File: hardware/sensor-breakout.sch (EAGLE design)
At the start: 63 parts, among them IC1 ATMEGA168-MU, U1 MCP73831, U2 NRF24L01SMD, U4 MCP5301, Y1 16M, Y2 12MHz

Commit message: hw: update values
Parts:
- R1: value TBD -> 3k9
- R2: value 2k2 -> 1k5
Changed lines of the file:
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@@
 <part name="GND6" library="supply1" deviceset="GND" device=""/>
 <part name="GND2" library="supply1" deviceset="GND" device=""/>
-<part name="R2" library="rcl" deviceset="R-EU_" device="R0603" value="2k2"/>
+<part name="R2" library="rcl" deviceset="R-EU_" device="R0603" value="1k5"/>
 <part name="R3" library="rcl" deviceset="R-EU_" device="R0603" value="68"/>
 <part name="R4" library="rcl" deviceset="R-EU_" device="R0603" value="68"/>
 <part name="U1" library="SparkFun-PowerIC" deviceset="MCP73831" device=""/>
-<part name="R1" library="rcl" deviceset="R-EU_" device="R0603" value="TBD"/>
+<part name="R1" library="rcl" deviceset="R-EU_" device="R0603" value="3k9"/>
 <part name="GND1" library="supply1" deviceset="GND" device=""/>
 <part name="R5" library="rcl" deviceset="R-EU_" device="R0603" value="5k6"/>

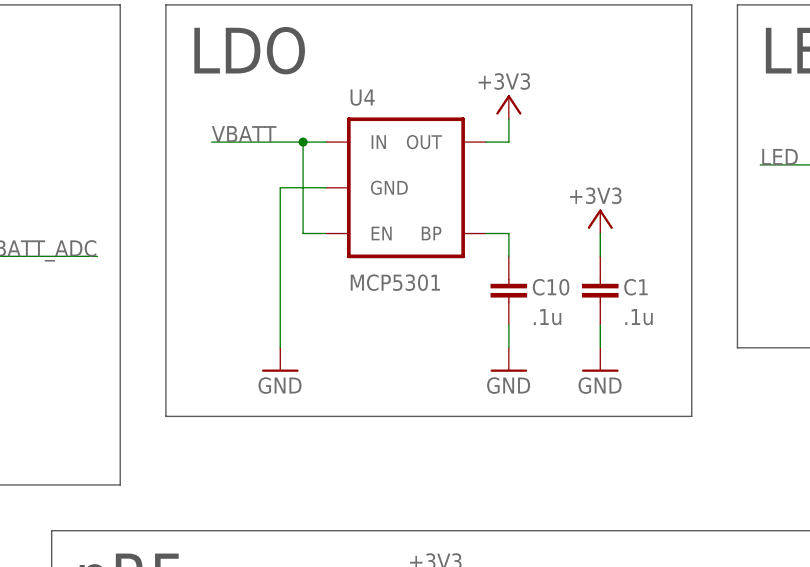
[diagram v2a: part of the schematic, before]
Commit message: hw: fix ldo part number
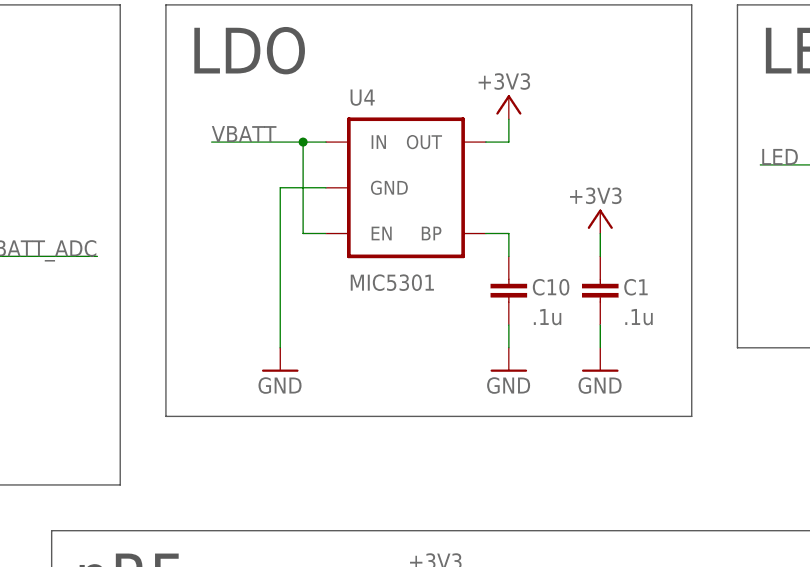
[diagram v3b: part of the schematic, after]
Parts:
- U4: value MCP5301 -> MIC5301
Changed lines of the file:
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@@
 <part name="P+6" library="supply1" deviceset="+5V" device=""/>
 <part name="GND4" library="supply1" deviceset="GND" device=""/>
-<part name="U4" library="SparkFun-PowerIC" deviceset="V_REG_LDO" device="SMD" value="MCP5301"/>
+<part name="U4" library="SparkFun-PowerIC" deviceset="V_REG_LDO" device="SMD" value="MIC5301"/>
 <part name="GND10" library="supply1" deviceset="GND" device=""/>
 <part name="C4" library="rcl" deviceset="C-EU" device="C0603" value="1u"/>
